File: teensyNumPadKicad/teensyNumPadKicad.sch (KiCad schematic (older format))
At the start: 37 parts, among them U1 Teensy++2.0_(C)

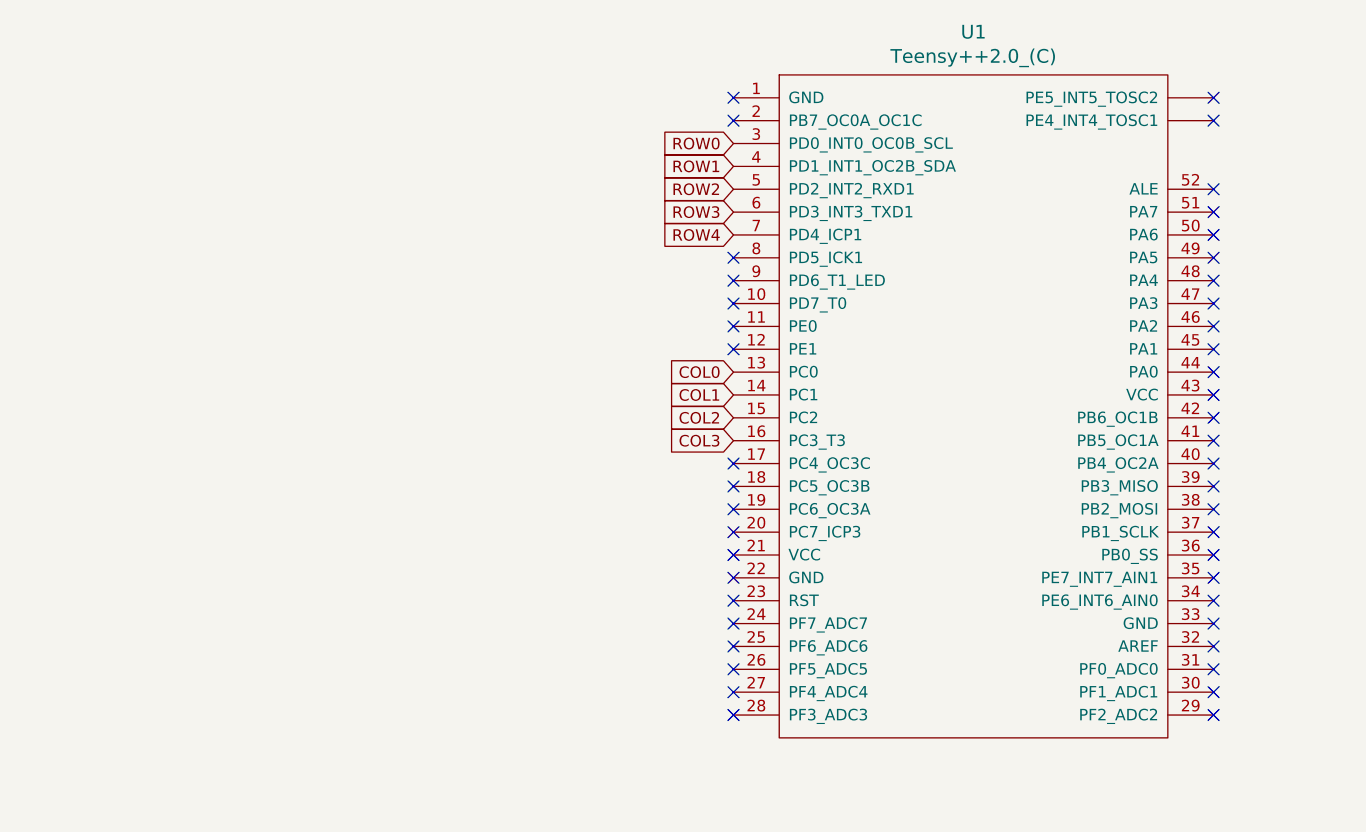
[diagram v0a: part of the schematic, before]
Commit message: Add 5 pin din plug for connection to an Amiga
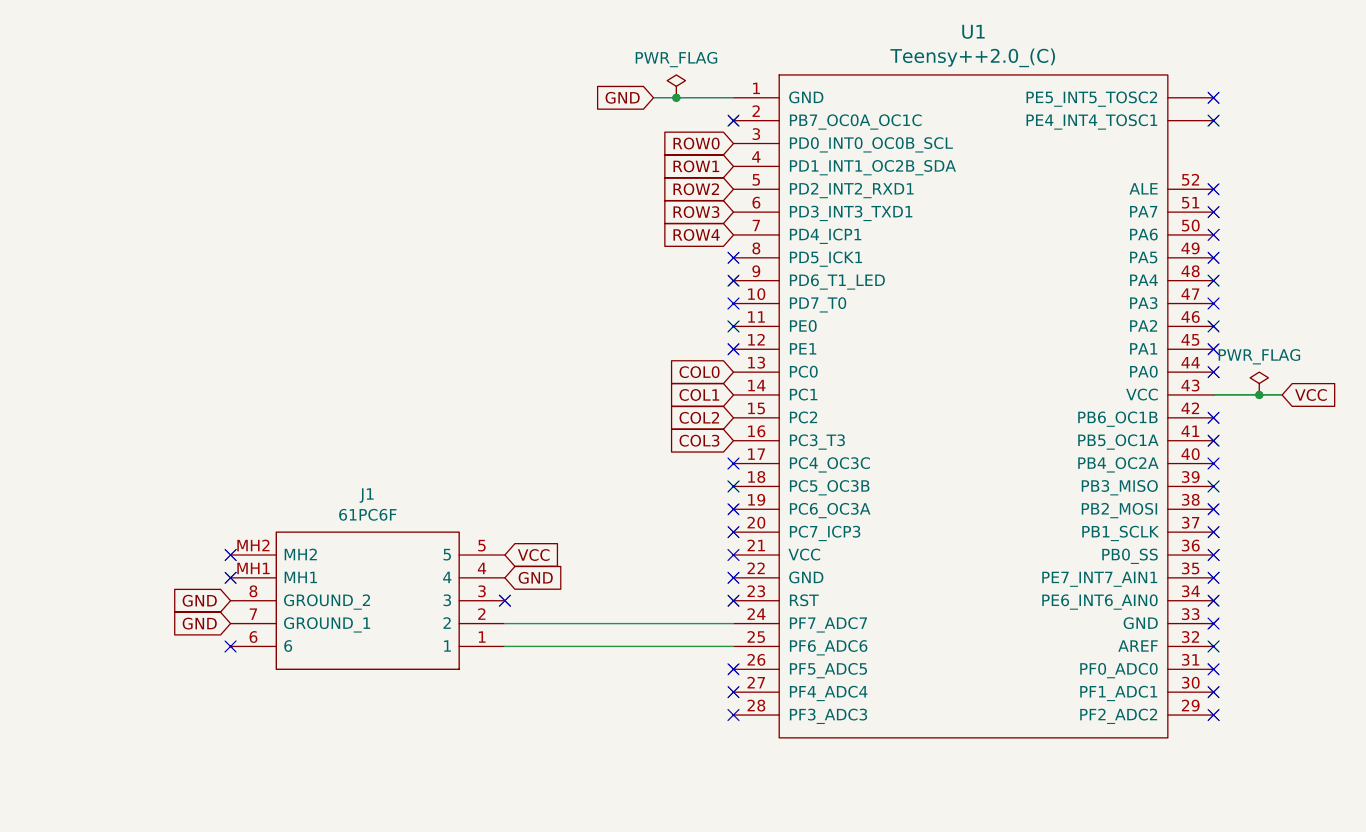
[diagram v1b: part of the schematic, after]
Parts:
- added J1: 61PC6F, SamacSys_Parts:61PC6F, symbol SamacSys_Parts:61PC6F
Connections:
- net GND: now reaches U1.1 (GND)
- net GND: now also J1.4, J1.7 (GROUND_1), J1.8 (GROUND_2)
- net at U1.24 (PF7_ADC7): now also J1.2
- net at U1.25 (PF6_ADC6): now also J1.1
- net VCC: now reaches U1.43 (VCC)
- net VCC: now also J1.5
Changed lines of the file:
@@
 EESchema Schematic File Version 4
+LIBS:teensyNumPadKicad-cache
 EELAYER 30 0
 EELAYER END
@@
 Text GLabel 7350 3100 0    50   Input ~ 0
 COL3
-NoConn ~ 7350 1600
 NoConn ~ 7350 1700
 NoConn ~ 7350 2300
@@
 NoConn ~ 7350 3200
 NoConn ~ 7350 3300
-NoConn ~ 7350 3400
-NoConn ~ 7350 3500
-NoConn ~ 7350 3600
-NoConn ~ 7350 3700
 NoConn ~ 7350 3800
-NoConn ~ 7350 3900
-NoConn ~ 7350 4000
 NoConn ~ 7350 4100
 NoConn ~ 7350 4200
@@
 NoConn ~ 9450 2700
 NoConn ~ 9450 2800
-NoConn ~ 9450 2900
 NoConn ~ 9450 3000
 NoConn ~ 9450 3100
@@
 	1    0    0    -1
 $EndComp
+$Comp
+L SamacSys_Parts:61PC6F J1
+U 1 1 60901334
+P 6350 4000
+F 0 "J1" H 6950 3335 50  0000 C CNN
+F 1 "61PC6F" H 6950 3426 50  0000 C CNN
+F 2 "SamacSys_Parts:61PC6F" H 7400 4100 50  0001 L CNN
+F 3 "http://www.switchcraft.com/Drawings/61PC6F_CD.pdf" H 7400 4000 50  0001 L CNN
+F 4 "Conn Circular DIN F 6 POS Solder RA Thru-Hole 6 Terminal 1 Port" H 7400 3900 50  0001 L CNN "Description"
+F 5 "21" H 7400 3800 50  0001 L CNN "Height"
+F 6 "502-61PC6F" H 7400 3700 50  0001 L CNN "Mouser Part Number"
+F 7 "https://www.mouser.co.uk/ProductDetail/Switchcraft/61PC6F?qs=I3kMT7EEIOX5qfso%2F%2FYu%2Fg%3D%3D" H 7400 3600 50  0001 L CNN "Mouser Price/Stock"
+F 8 "Switchcraft" H 7400 3500 50  0001 L CNN "Manufacturer_Name"
+F 9 "61PC6F" H 7400 3400 50  0001 L CNN "Manufacturer_Part_Number"
+	1    6350 4000
+	-1   0    0    1
+$EndComp
+NoConn ~ 6350 3800
+Text GLabel 6350 3700 2    50   Input ~ 0
+GND
+Text GLabel 5150 3800 0    50   Input ~ 0
+GND
+Text GLabel 5150 3900 0    50   Input ~ 0
+GND
+NoConn ~ 5150 4000
+NoConn ~ 5150 3600
+NoConn ~ 5150 3700
+Text GLabel 7000 1600 0    50   Input ~ 0
+GND
+$Comp
+L power:PWR_FLAG #FLG0102
+U 1 1 6092CC8F
+P 7100 1600
+F 0 "#FLG0102" H 7100 1675 50  0001 C CNN
+F 1 "PWR_FLAG" H 7100 1773 50  0000 C CNN
+F 2 "" H 7100 1600 50  0001 C CNN
+F 3 "~" H 7100 1600 50  0001 C CNN
+	1    7100 1600
+	1    0    0    -1
+$EndComp
+Connection ~ 7100 1600
+Wire Wire Line
+	7100 1600 7000 1600
+Wire Wire Line
+	7100 1600 7350 1600
+NoConn ~ 7350 3700
+NoConn ~ 7350 3600
+Text GLabel 6350 3600 2    50   Input ~ 0
+VCC
+Wire Wire Line
+	9450 2900 9650 2900
+Text GLabel 9750 2900 2    50   Input ~ 0
+VCC
+$Comp
+L power:PWR_FLAG #FLG?
+U 1 1 6094D3F7
+P 9650 2900
+F 0 "#FLG?" H 9650 2975 50  0001 C CNN
+F 1 "PWR_FLAG" H 9650 3073 50  0000 C CNN
+F 2 "" H 9650 2900 50  0001 C CNN
+F 3 "~" H 9650 2900 50  0001 C CNN
+	1    9650 2900
+	1    0    0    -1
+$EndComp
+Connection ~ 9650 2900
+Wire Wire Line
+	9650 2900 9750 2900
+NoConn ~ 7350 3400
+NoConn ~ 7350 3500
+Wire Wire Line
+	7350 3900 6350 3900
+Wire Wire Line
+	7350 4000 6350 4000
 $EndSCHEMATC

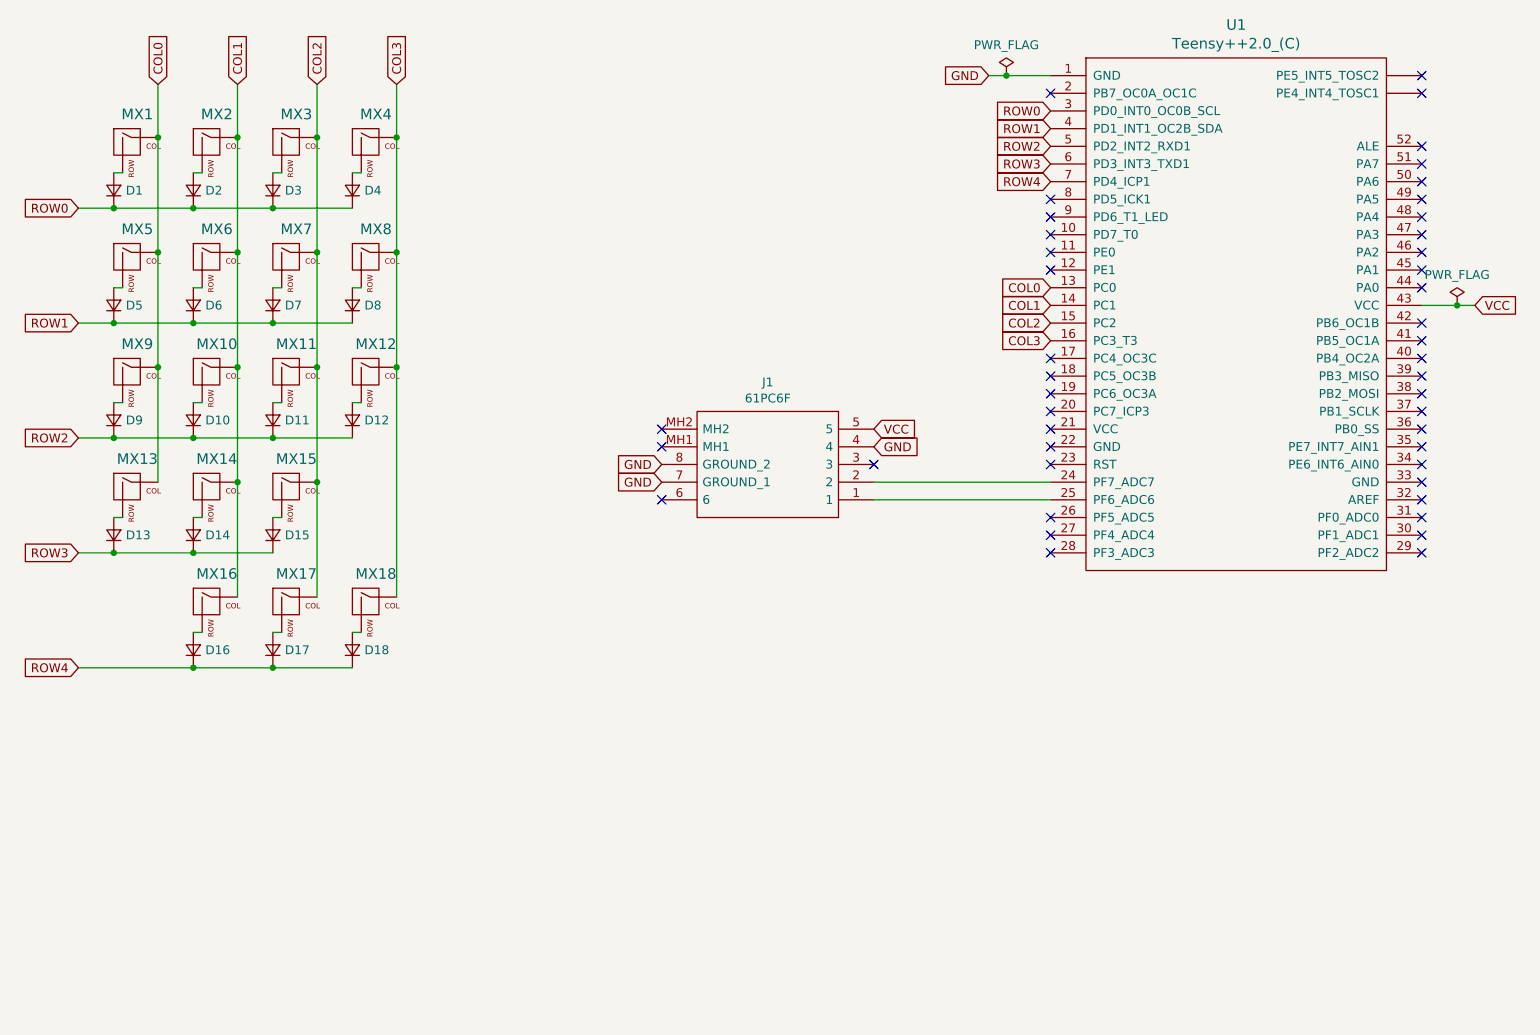
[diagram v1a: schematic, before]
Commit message: Add Modifier keys + LEDs
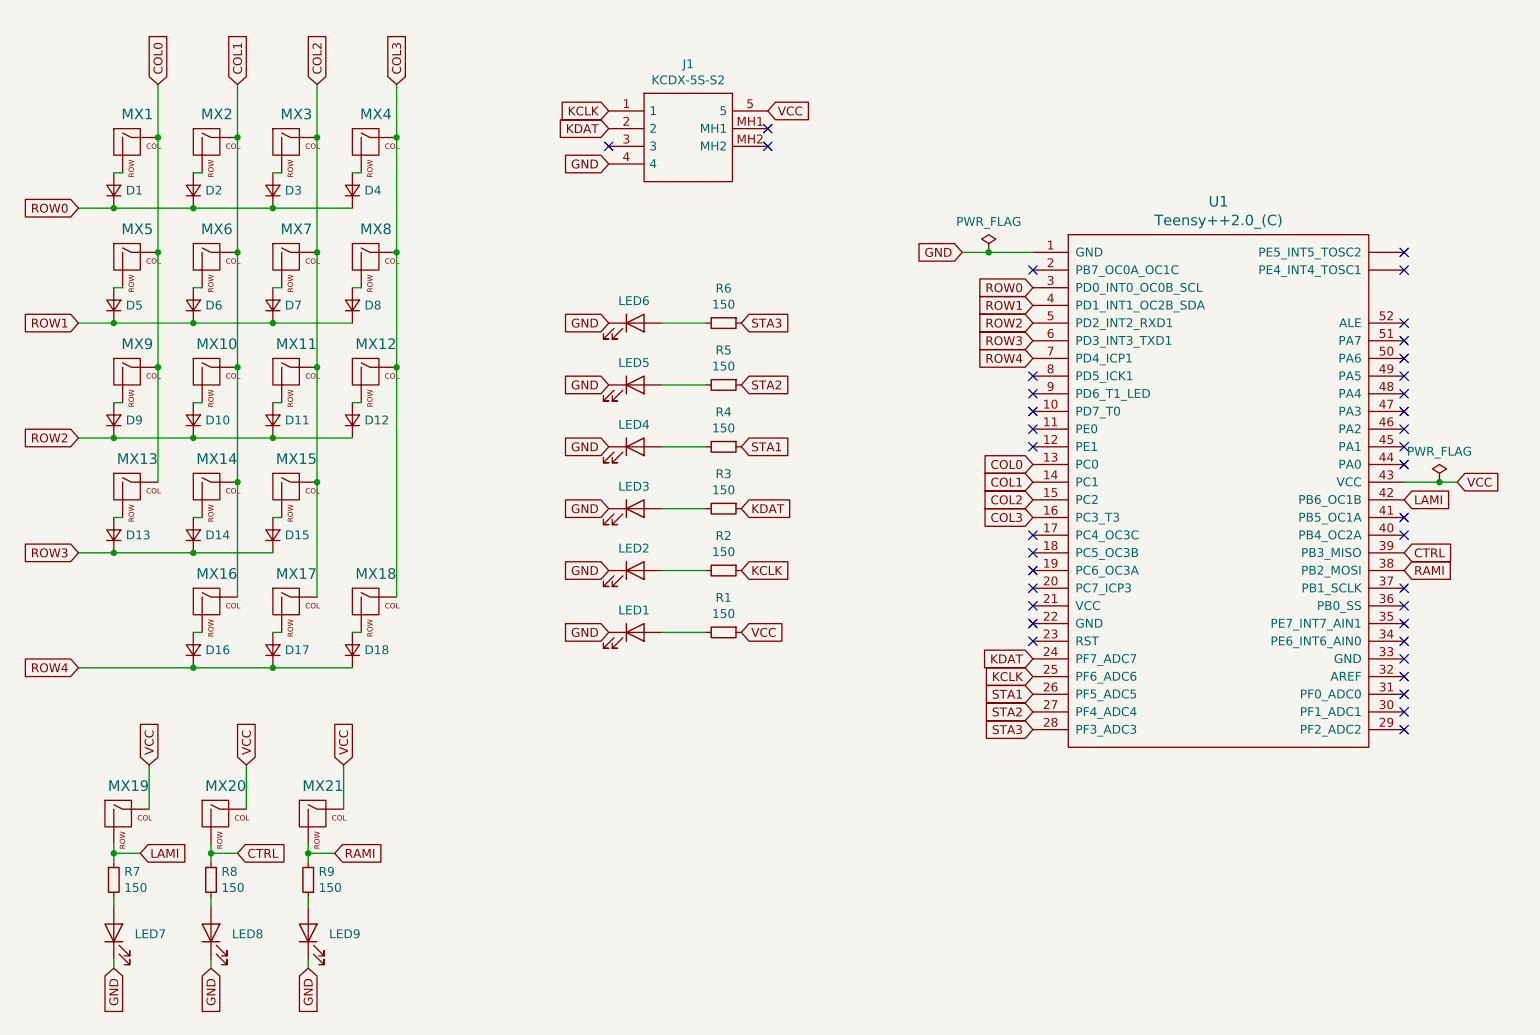
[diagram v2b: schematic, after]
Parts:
- removed J1: 61PC6F, SamacSys_Parts:61PC6F, symbol SamacSys_Parts:61PC6F
- added J1: KCDX-5S-S2, SamacSys_Parts:KCDX5SS2, symbol SamacSys_Parts:KCDX-5S-S2
- added LED1, LED2, LED3, LED4, LED5, LED6, LED7, LED8, LED9: LED, LED_THT:LED_D3.0mm, symbol Device:LED
- added MX19, MX20, MX21: MX-NoLED, MX_Alps_Hybrid:MX-1.25U-NoLED, symbol MX_Alps_Hybrid:MX-NoLED
- added R1, R2, R3, R4, R5, R6, R7, R8, R9: 150, Resistor_THT:R_Axial_DIN0207_L6.3mm_D2.5mm_P7.62mm_Horizontal, symbol Device:R_Small
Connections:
- net GND: now also J1.4, LED1.1 (K), LED2.1 (K), LED3.1 (K), LED4.1 (K), LED5.1 (K), LED6.1 (K), LED7.1 (K), LED8.1 (K), LED9.1 (K)
- net VCC: now also J1.5, MX19.1 (COL), MX20.1 (COL), MX21.1 (COL), R1.1
- net KDAT: now reaches U1.24 (PF7_ADC7)
- net KDAT: now also J1.2, R3.1
- net KCLK: now reaches U1.25 (PF6_ADC6)
- net KCLK: now also J1.1, R2.1
- net STA1: now reaches U1.26 (PF5_ADC5)
- net STA1: now also R4.1
- net STA2: now reaches U1.27 (PF4_ADC4)
- net STA2: now also R5.1
- net STA3: now reaches U1.28 (PF3_ADC3)
- net STA3: now also R6.1
- net RAMI: now reaches U1.38 (PB2_MOSI)
- net RAMI: now also MX21.2 (ROW), R9.2
- net CTRL: now reaches U1.39 (PB3_MISO)
- net CTRL: now also MX20.2 (ROW), R8.1
- net LAMI: now reaches U1.42 (PB6_OC1B)
- net LAMI: now also MX19.2 (ROW), R7.1
- new net: LED1.2 (A), R1.2
- new net: LED2.2 (A), R2.2
- new net: LED3.2 (A), R3.2
- new net: LED4.2 (A), R4.2
- new net: LED5.2 (A), R5.2
- new net: LED6.2 (A), R6.2
- new net: LED7.2 (A), R7.2
- new net: LED8.2 (A), R8.2
- new net: LED9.2 (A), R9.1
- no-connect marks 45 -> 38
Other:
- moved on the sheet: U1

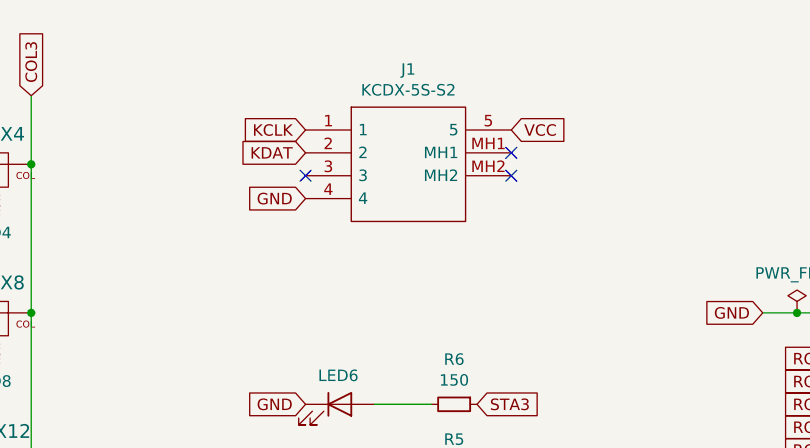
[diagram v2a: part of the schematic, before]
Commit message: Updated Schema and PCB
Fixed pin assignments on 5 pin DIN socket as follows:
1      Not Connected
2      KDAT
3      KCLK
4      +5V
5      GND
This is because the pins are numbered from right to left rather than left to right.  Also increased the size of the resistor footprints.
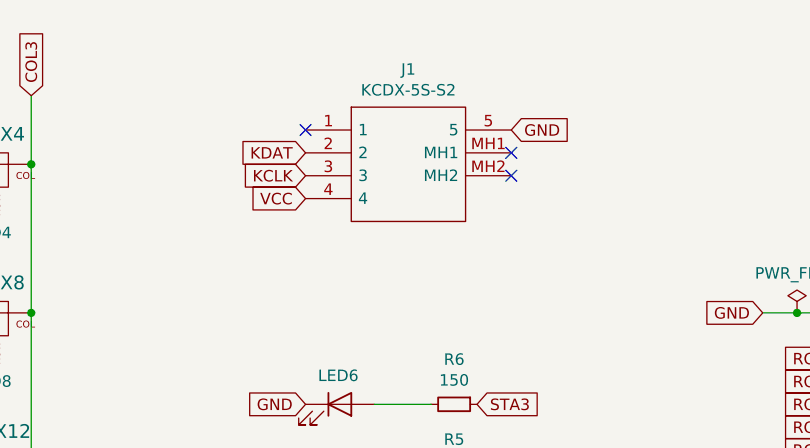
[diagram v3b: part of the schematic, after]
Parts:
- R1, R2, R3, R4, R5, R6, R7, R8, R9: footprint Resistor_THT:R_Axial_DIN0207_L6.3mm_D2.5mm_P7.62mm_Horizontal -> Resistor_THT:R_Axial_DIN0207_L6.3mm_D2.5mm_P10.16mm_Horizontal
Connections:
- net GND: now also J1.5; no longer J1.4
- net KCLK: now also J1.3; no longer J1.1
- net VCC: now also J1.4; no longer J1.5
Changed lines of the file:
@@
 Text GLabel 7250 5000 0    50   Input ~ 0
 KCLK
-Text GLabel 4850 1800 0    50   Input ~ 0
+Text GLabel 4850 2000 0    50   Input ~ 0
 KCLK
-NoConn ~ 4850 2000
 $Comp
 L Device:LED LED1
@@
 F 0 "R1" V 5304 4750 50  0000 C CNN
 F 1 "150" V 5395 4750 50  0000 C CNN
-F 2 "Resistor_THT:R_Axial_DIN0207_L6.3mm_D2.5mm_P7.62mm_Horizontal" H 5500 4750 50  0001 C CNN
+F 2 "Resistor_THT:R_Axial_DIN0207_L6.3mm_D2.5mm_P10.16mm_Horizontal" H 5500 4750 50  0001 C CNN
 F 3 "~" H 5500 4750 50  0001 C CNN
 	1    5500 4750
@@
 Wire Wire Line
 	5400 4750 5150 4750
+Text GLabel 5750 1800 2    50   Input ~ 0
+GND
+Text GLabel 4850 4750 0    50   Input ~ 0
+GND
+Text GLabel 6850 2600 0    50   Input ~ 0
+GND
 Text GLabel 4850 2100 0    50   Input ~ 0
-GND
-Text GLabel 4850 4750 0    50   Input ~ 0
-GND
-Text GLabel 6850 2600 0    50   Input ~ 0
-GND
-Text GLabel 5750 1800 2    50   Input ~ 0
 VCC
 Text GLabel 5600 4750 2    50   Input ~ 0
@@
 F 0 "R2" V 5304 4400 50  0000 C CNN
 F 1 "150" V 5395 4400 50  0000 C CNN
-F 2 "Resistor_THT:R_Axial_DIN0207_L6.3mm_D2.5mm_P7.62mm_Horizontal" H 5500 4400 50  0001 C CNN
+F 2 "Resistor_THT:R_Axial_DIN0207_L6.3mm_D2.5mm_P10.16mm_Horizontal" H 5500 4400 50  0001 C CNN
 F 3 "~" H 5500 4400 50  0001 C CNN
 	1    5500 4400
@@
 F 0 "R3" V 5304 4050 50  0000 C CNN
 F 1 "150" V 5395 4050 50  0000 C CNN
-F 2 "Resistor_THT:R_Axial_DIN0207_L6.3mm_D2.5mm_P7.62mm_Horizontal" H 5500 4050 50  0001 C CNN
+F 2 "Resistor_THT:R_Axial_DIN0207_L6.3mm_D2.5mm_P10.16mm_Horizontal" H 5500 4050 50  0001 C CNN
 F 3 "~" H 5500 4050 50  0001 C CNN
 	1    5500 4050
@@
 F 0 "R4" V 5304 3700 50  0000 C CNN
 F 1 "150" V 5395 3700 50  0000 C CNN
-F 2 "Resistor_THT:R_Axial_DIN0207_L6.3mm_D2.5mm_P7.62mm_Horizontal" H 5500 3700 50  0001 C CNN
+F 2 "Resistor_THT:R_Axial_DIN0207_L6.3mm_D2.5mm_P10.16mm_Horizontal" H 5500 3700 50  0001 C CNN
 F 3 "~" H 5500 3700 50  0001 C CNN
 	1    5500 3700
@@
 F 0 "R5" V 5304 3350 50  0000 C CNN
 F 1 "150" V 5395 3350 50  0000 C CNN
-F 2 "Resistor_THT:R_Axial_DIN0207_L6.3mm_D2.5mm_P7.62mm_Horizontal" H 5500 3350 50  0001 C CNN
+F 2 "Resistor_THT:R_Axial_DIN0207_L6.3mm_D2.5mm_P10.16mm_Horizontal" H 5500 3350 50  0001 C CNN
 F 3 "~" H 5500 3350 50  0001 C CNN
 	1    5500 3350
@@
 F 0 "R6" V 5304 3000 50  0000 C CNN
 F 1 "150" V 5395 3000 50  0000 C CNN
-F 2 "Resistor_THT:R_Axial_DIN0207_L6.3mm_D2.5mm_P7.62mm_Horizontal" H 5500 3000 50  0001 C CNN
+F 2 "Resistor_THT:R_Axial_DIN0207_L6.3mm_D2.5mm_P10.16mm_Horizontal" H 5500 3000 50  0001 C CNN
 F 3 "~" H 5500 3000 50  0001 C CNN
 	1    5500 3000
@@
 F 0 "R7" H 2109 6196 50  0000 L CNN
 F 1 "150" H 2109 6105 50  0000 L CNN
-F 2 "Resistor_THT:R_Axial_DIN0207_L6.3mm_D2.5mm_P7.62mm_Horizontal" H 2050 6150 50  0001 C CNN
+F 2 "Resistor_THT:R_Axial_DIN0207_L6.3mm_D2.5mm_P10.16mm_Horizontal" H 2050 6150 50  0001 C CNN
 F 3 "~" H 2050 6150 50  0001 C CNN
 	1    2050 6150
@@
 F 0 "R8" H 2659 6196 50  0000 L CNN
 F 1 "150" H 2659 6105 50  0000 L CNN
-F 2 "Resistor_THT:R_Axial_DIN0207_L6.3mm_D2.5mm_P7.62mm_Horizontal" H 2600 6150 50  0001 C CNN
+F 2 "Resistor_THT:R_Axial_DIN0207_L6.3mm_D2.5mm_P10.16mm_Horizontal" H 2600 6150 50  0001 C CNN
 F 3 "~" H 2600 6150 50  0001 C CNN
 	1    2600 6150
@@
 F 0 "R9" H 3091 6104 50  0000 R CNN
 F 1 "150" H 3091 6195 50  0000 R CNN
-F 2 "Resistor_THT:R_Axial_DIN0207_L6.3mm_D2.5mm_P7.62mm_Horizontal" H 3150 6150 50  0001 C CNN
+F 2 "Resistor_THT:R_Axial_DIN0207_L6.3mm_D2.5mm_P10.16mm_Horizontal" H 3150 6150 50  0001 C CNN
 F 3 "~" H 3150 6150 50  0001 C CNN
 	1    3150 6150
@@
 Text GLabel 9350 4400 2    50   Input ~ 0
 RAMI
+NoConn ~ 4850 1800
 $EndSCHEMATC
